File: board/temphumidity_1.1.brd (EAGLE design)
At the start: 38.1 x 61.2 mm, 33 parts, among them J1 10118192-0001LF, J2 B2B-PH-K-S(LF)(SN), Q1 MMBT2222A, Q2 MMBT2222A, U1 ENS210-LQFM, U2 ESP-WROOM-02, U3 FT231XS-U

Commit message: More revisions on 1.1, added pictures for Readme
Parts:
- removed JP2: (no value), pinhead:1X03
- added R15: 4.7k, rcl:R0805
- added R16: 10k, rcl:R0805
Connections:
- net 3V3: no longer JP2.1
- net ADC: now also R15.2, R16.1; no longer JP2.2
- net GND: now also R16.2; no longer JP2.3
- net VBAT: now also R15.1
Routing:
- net VBAT: track 53.3 -> 85.2 mm
- net 3V3: track 131.0 -> 110.2 mm
- net ADC: track 6.65 -> 11.0 mm
- net N$15: track 14.4 -> 16.1 mm
- net N$14: track 17.3 -> 18.7 mm
- net GND: track 319.8 -> 320.8 mm
- net N$6: track 20.3 -> 21.2 mm, vias 0 -> 2
- added copper zone on layer 1, net 3V3
- added copper zone on layer 1, net SELECTEDVOLTAGE
- added copper zone on layer 1, net VBAT
- added copper zone on layer 1, net VUSB

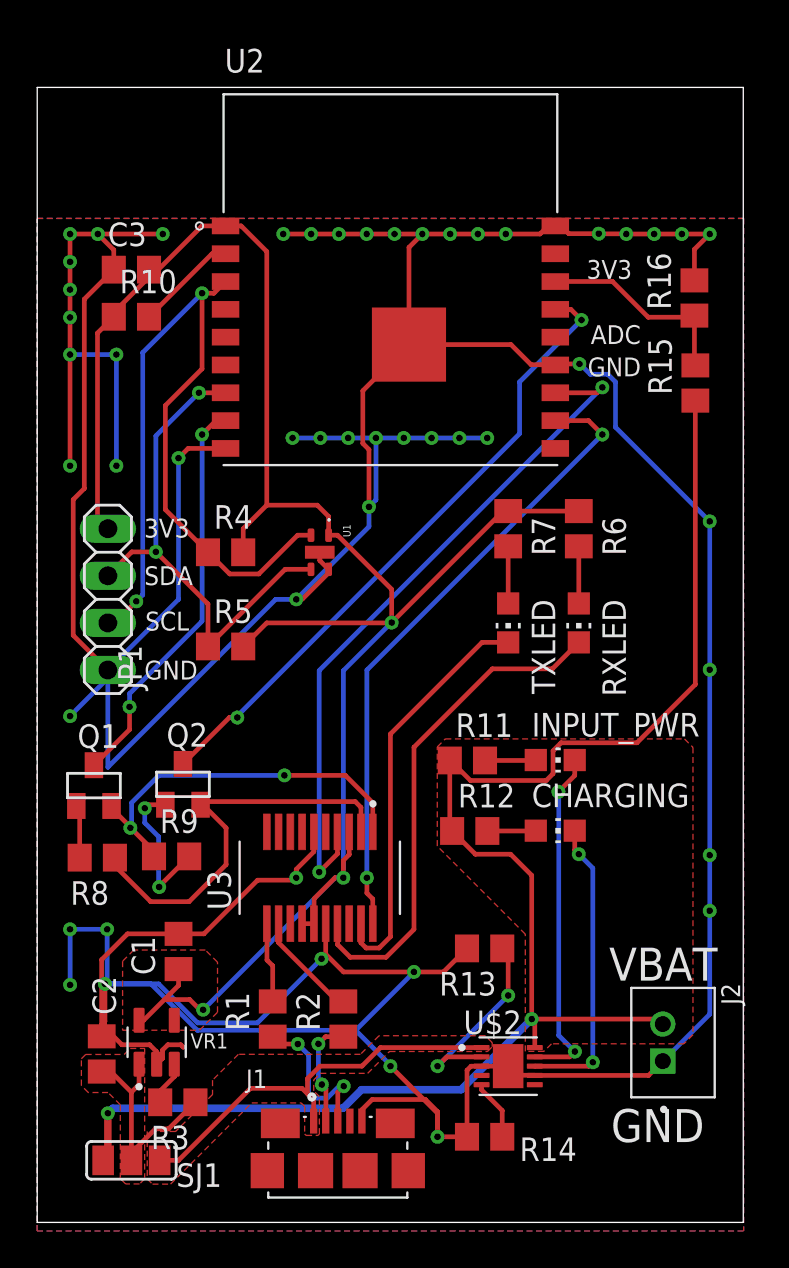
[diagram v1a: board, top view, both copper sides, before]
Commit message: Wrote spring application to make use of sql database
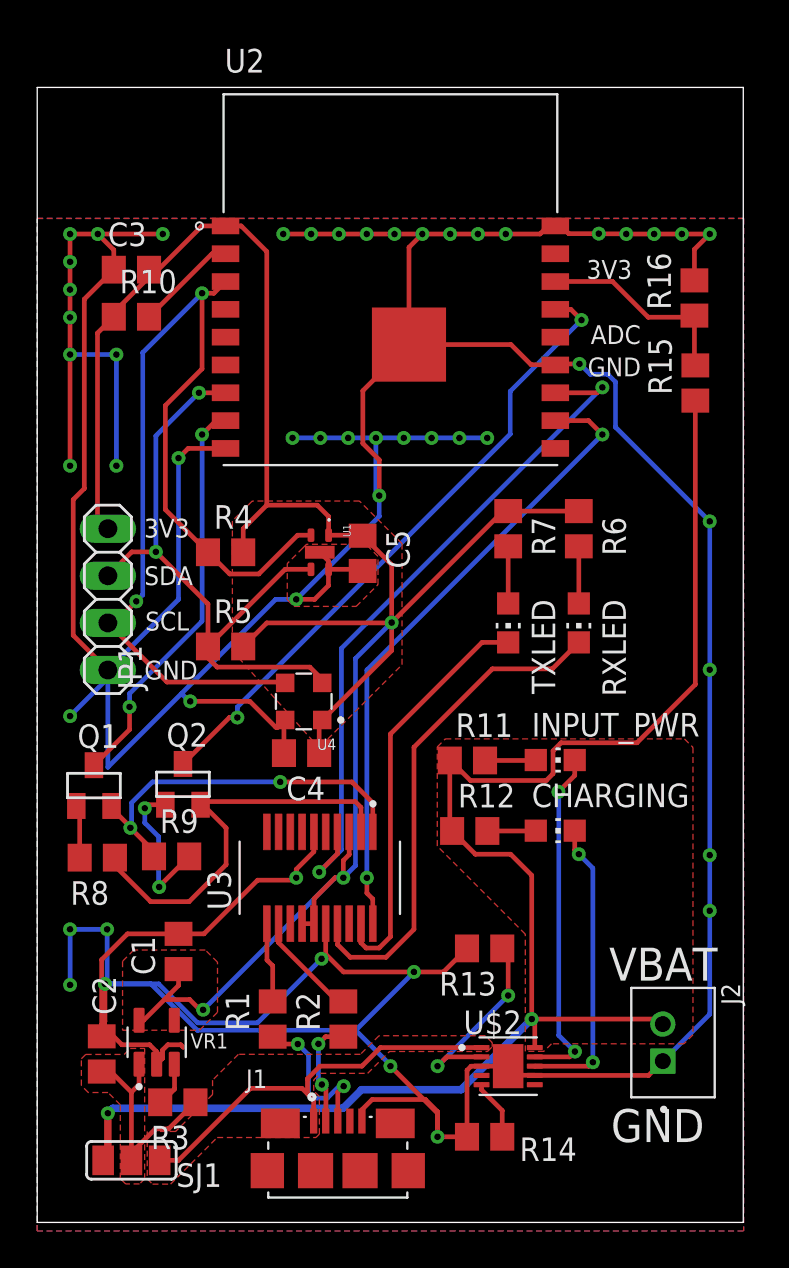
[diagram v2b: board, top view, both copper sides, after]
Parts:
- added C4, C5: 1uF, rcl:C0805
- added U4: MS563702BA03-50, MS563702BA03-50:TE_MS563702BA03-50
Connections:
- net 3V3: now also C4.1, C5.1, U4.1
- net GND: now also C4.2, C5.2, U4.4
- net SCL: now also U4.3
- net SDA: now also U4.2
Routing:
- net SCL: track 44.3 -> 55.2 mm
- net GND: track 320.8 -> 331.2 mm, vias 50 -> 51
- net 3V3: track 110.2 -> 119.7 mm
- net SDA: track 27.6 -> 35.1 mm
- net N$6: track 21.2 -> 20.6 mm

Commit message: More board work
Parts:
- moved R6 4.92 mm to (23.9, 33.8)
- moved RXLED 4.92 mm to (23.9, 28.7)
- moved R7 4.92 mm to (20.1, 33.8)
- moved TXLED 4.92 mm to (20.1, 28.7)
- moved R15 3.89 mm to (30.6, 45.8)
- moved R16 3.78 mm to (30.5, 50.0)
- moved J2 1.84 mm to (31.2, 8.73)
- moved R13 1.67 mm to (21.7, 12.7)
- moved U3 0.46 mm to (14.0, 17.3)
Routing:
- net GND: track 331.2 -> 319.6 mm, vias 51 -> 48
- net N$7: track 27.2 -> 22.1 mm
- net ADC: track 11.0 -> 6.63 mm
- net N$8: track 22.3 -> 18.5 mm
- net 3V3: track 119.7 -> 116.0 mm
- net VBAT: track 85.2 -> 82.0 mm
- net N$15: track 16.1 -> 14.7 mm
- net N$14: track 18.7 -> 17.4 mm
- net N$17: track 10.6 -> 9.95 mm
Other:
- board size 38.1 x 61.2 mm -> 33.7 x 61.3 mm

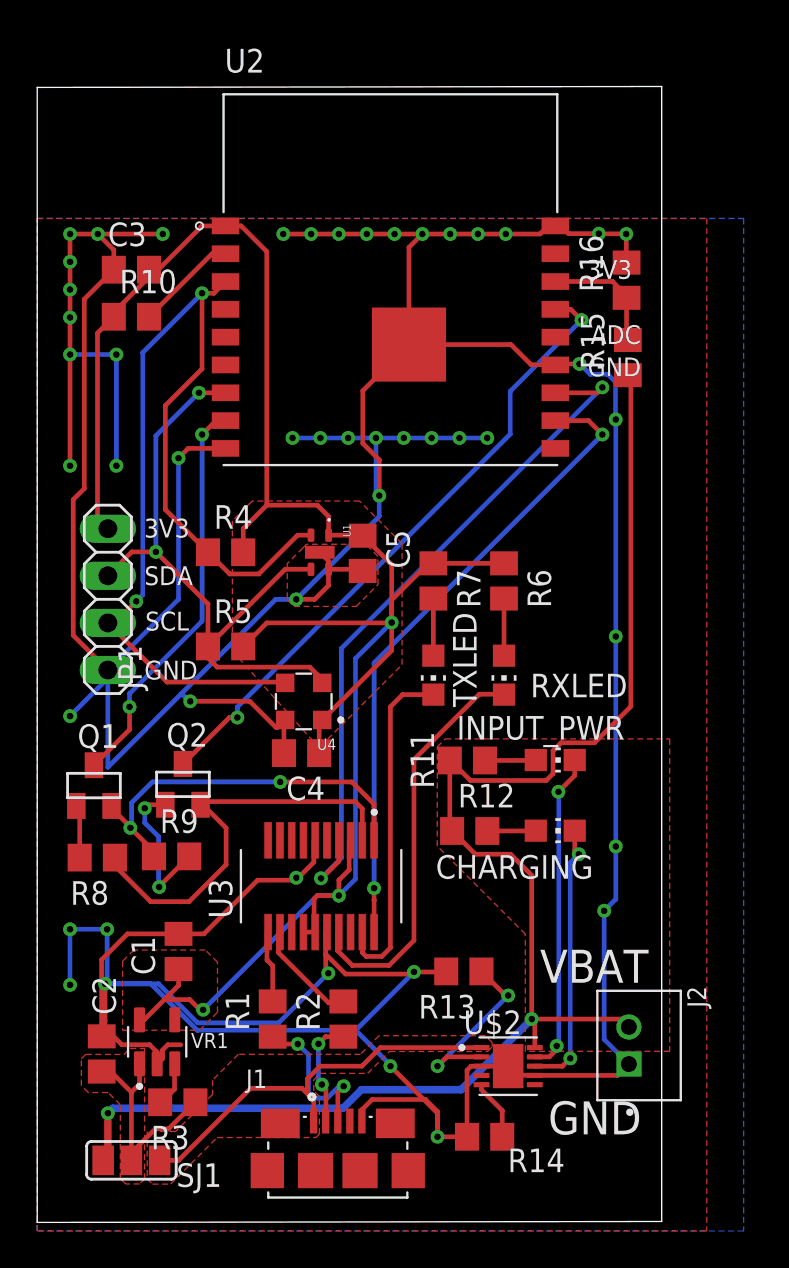
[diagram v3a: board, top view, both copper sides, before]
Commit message: Added breakout so old programmers can program new boards
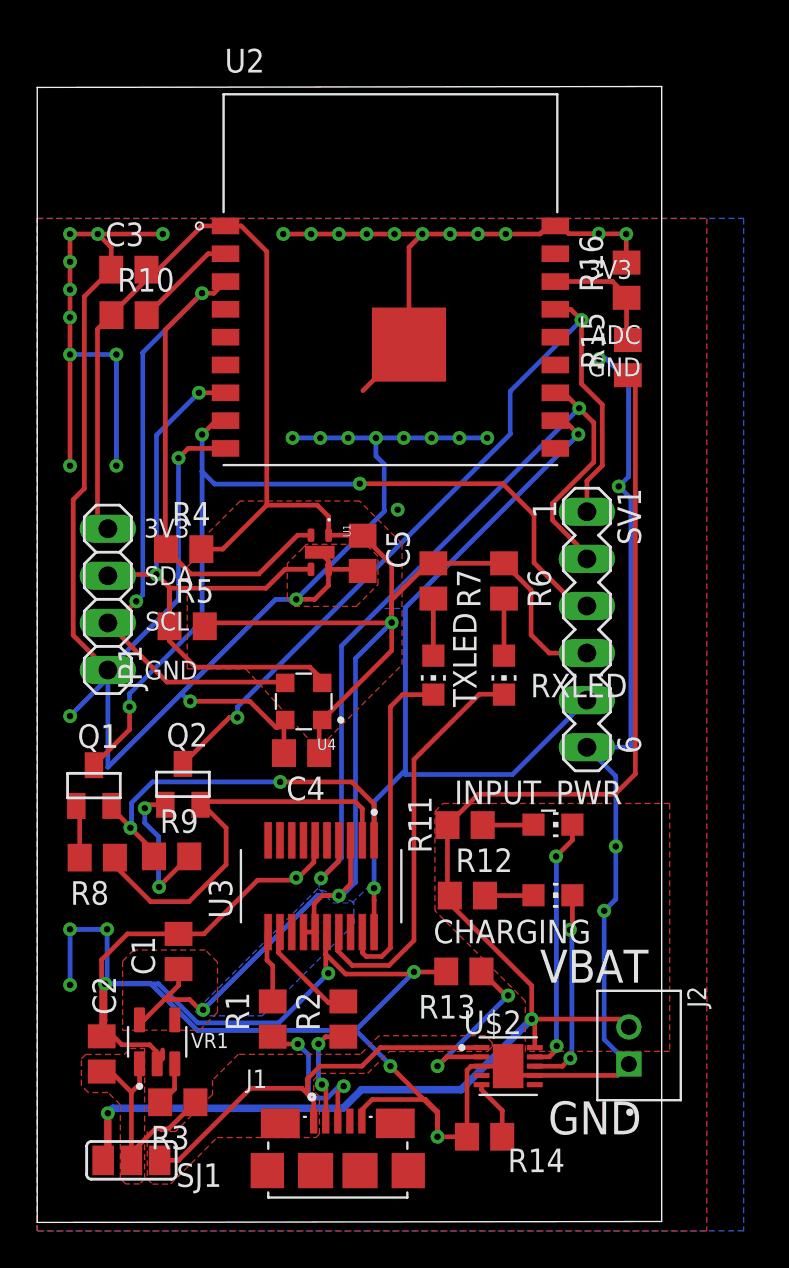
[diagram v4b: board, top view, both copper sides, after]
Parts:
- added SV1: (no value), con-lstb:MA06-1
- moved CHARGING 3.49 mm to (26.5, 16.8)
- moved INPUT_PWR 3.49 mm to (26.5, 20.6)
- moved R11 3.49 mm to (21.8, 20.6)
- moved R12 3.49 mm to (21.9, 16.8)
- moved R5 2.34 mm to (6.82, 31.3)
- moved R4 2.26 mm to (6.63, 35.5)
- moved R10 0.15 mm to (3.68, 48.1)
- moved C3 0.14 mm to (3.67, 50.6)
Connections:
- net N$4 renamed RTS
- net N$6 renamed DTR
- net 3V3: now also SV1.4
- net BOOT: now also SV1.3
- net GND: now also SV1.6
- net RESET: now also SV1.1
- net UART_RX: now also SV1.2
- net UART_TX: now also SV1.5
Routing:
- net BOOT: track 21.8 -> 47.1 mm, vias 2 -> 3
- net GND: track 319.6 -> 306.2 mm, vias 48 -> 47
- net RESET: track 34.7 -> 45.9 mm
- net 3V3: track 116.0 -> 127.0 mm
- net UART_TX: track 34.8 -> 44.6 mm
- net UART_RX: track 37.9 -> 45.4 mm
- net N$15: track 14.7 -> 11.0 mm
- net N$14: track 17.4 -> 13.9 mm
- net SDA: track 35.1 -> 38.1 mm
- net VBAT: track 82.0 -> 79.9 mm
- net SCL: track 55.2 -> 56.4 mm
- added copper zone on layer 16, net 3V3
